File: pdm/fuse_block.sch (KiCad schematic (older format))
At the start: 14 parts, among them Q12 2N7002E, Q13 2N7002E, Q14 2N7002E, U5 BTS443P

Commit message: general changes
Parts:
- added TP6, TP7, TP8: TestPoint, TestPoint:TestPoint_THTPad_1.0x1.0mm_Drill0.5mm, symbol Connector:TestPoint
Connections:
- net Vout: now also TP7.1
- net activate: now also TP6.1
- net sense: now also TP8.1
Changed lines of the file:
@@
 $Descr A4 11693 8268
 encoding utf-8
-Sheet 6 6
+Sheet 3 6
 Title "PDM Board"
 Date "2021-01-14"
@@
 Connection ~ 7950 3600
 Wire Wire Line
-	7950 3600 9050 3600
+	7950 3600 8700 3600
 Text HLabel 9050 3600 2    50   Output ~ 0
 Vout
@@
 Connection ~ 7600 2450
 Wire Wire Line
-	7600 2450 9050 2450
-Wire Wire Line
-	3000 3700 4550 3700
+	3000 3700 3450 3700
 Wire Wire Line
 	7950 4900 8450 4900
@@
 Wire Wire Line
 	8850 3900 8850 4300
+$Comp
+L Connector:TestPoint TP7
+U 1 1 60F5EFD6
+P 8700 3300
+AR Path="/5F94FFF3/60F5EFD6" Ref="TP7"  Part="1"
+AR Path="/5F955F6E/60F5EFD6" Ref="TP4"  Part="1"
+AR Path="/5F955EE4/60F5EFD6" Ref="TP10"  Part="1"
+AR Path="/60D2AFFB/60F5EFD6" Ref="TP13"  Part="1"
+F 0 "TP13" H 8758 3418 50  0000 L CNN
+F 1 "TestPoint" H 8758 3327 50  0000 L CNN
+F 2 "TestPoint:TestPoint_THTPad_1.0x1.0mm_Drill0.5mm" H 8900 3300 50  0001 C CNN
+F 3 "~" H 8900 3300 50  0001 C CNN
+	1    8700 3300
+	1    0    0    -1
+$EndComp
+Wire Wire Line
+	8700 3300 8700 3600
+Connection ~ 8700 3600
+Wire Wire Line
+	8700 3600 9050 3600
+Wire Wire Line
+	7600 2450 8700 2450
+$Comp
+L Connector:TestPoint TP6
+U 1 1 60F62FD8
+P 8700 2150
+AR Path="/5F94FFF3/60F62FD8" Ref="TP6"  Part="1"
+AR Path="/5F955F6E/60F62FD8" Ref="TP3"  Part="1"
+AR Path="/5F955EE4/60F62FD8" Ref="TP9"  Part="1"
+AR Path="/60D2AFFB/60F62FD8" Ref="TP12"  Part="1"
+F 0 "TP12" H 8758 2268 50  0000 L CNN
+F 1 "TestPoint" H 8758 2177 50  0000 L CNN
+F 2 "TestPoint:TestPoint_THTPad_1.0x1.0mm_Drill0.5mm" H 8900 2150 50  0001 C CNN
+F 3 "~" H 8900 2150 50  0001 C CNN
+	1    8700 2150
+	1    0    0    -1
+$EndComp
+Wire Wire Line
+	8700 2150 8700 2450
+Connection ~ 8700 2450
+Wire Wire Line
+	8700 2450 9050 2450
+$Comp
+L Connector:TestPoint TP8
+U 1 1 60F647E1
+P 3450 4000
+AR Path="/5F94FFF3/60F647E1" Ref="TP8"  Part="1"
+AR Path="/5F955F6E/60F647E1" Ref="TP5"  Part="1"
+AR Path="/5F955EE4/60F647E1" Ref="TP11"  Part="1"
+AR Path="/60D2AFFB/60F647E1" Ref="TP14"  Part="1"
+F 0 "TP14" H 3392 4026 50  0000 R CNN
+F 1 "TestPoint" H 3392 4117 50  0000 R CNN
+F 2 "TestPoint:TestPoint_THTPad_1.0x1.0mm_Drill0.5mm" H 3650 4000 50  0001 C CNN
+F 3 "~" H 3650 4000 50  0001 C CNN
+	1    3450 4000
+	-1   0    0    1
+$EndComp
+Wire Wire Line
+	3450 4000 3450 3700
+Connection ~ 3450 3700
+Wire Wire Line
+	3450 3700 4550 3700
 $EndSCHEMATC

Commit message: Initial commit
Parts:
- C13: Mouser PN 603-CC0805MKX58BB105 -> 80-C0603C160J3HACTU
- D4: Mouser PN 630-HSMR-C170-R0000 -> 710-150060AS75000
- F2: Mouser PN (none) -> 652-SF-1206F500M-2
- Q12, Q13, Q14: Mouser PN (none) -> 771-2N7002NXAKR
- R13: Mouser PN 603-AC0805FR-0710K5L -> 652-CRT0603FZ2002EST
- R19, R21, R25, R29: Mouser PN (none) -> 652-CRT0603FZ2002EST
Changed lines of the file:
@@
 F 3 "~" H 7150 2850 50  0001 C CNN
 F 4 "516-3541-1-ND" H 7150 2850 50  0001 C CNN "Digi-Key_PN"
-F 5 "630-HSMR-C170-R0000" H 7150 2850 50  0001 C CNN "Mouser PN"
+F 5 "710-150060AS75000" H 7150 2850 50  0001 C CNN "Mouser PN"
 	1    7150 2850
 	0    1    1    0
@@
 F 3 "~" H 4850 3500 50  0001 C CNN
 F 4 "RNCP0805FTD10K0CT-ND" H 4850 3500 50  0001 C CNN "Digi-Key_PN"
-F 5 "603-AC0805FR-0710K5L" H 4850 3500 50  0001 C CNN "Mouser PN"
+F 5 "652-CRT0603FZ2002EST" H 4850 3500 50  0001 C CNN "Mouser PN"
 	1    4850 3500
 	0    -1   -1   0
@@
 F 3 "~" H 4550 4050 50  0001 C CNN
 F 4 "1276-1859-2-ND" H 4550 4050 50  0001 C CNN "Digi-Key_PN"
-F 5 "603-CC0805MKX58BB105" H 4550 4050 50  0001 C CNN "Mouser PN"
+F 5 "80-C0603C160J3HACTU" H 4550 4050 50  0001 C CNN "Mouser PN"
 	1    4550 4050
 	1    0    0    -1
@@
 F 3 "~" H 6650 3600 50  0001 C CNN
 F 4 "486-1688-2-ND" H 6650 3600 50  0001 C CNN "Digi-Key_PN"
+F 5 "652-SF-1206F500M-2" H 6650 3600 50  0001 C CNN "Mouser PN"
 	1    6650 3600
 	0    1    1    0
@@
 F 3 "~" H 8450 5200 50  0001 C CNN
 F 4 "RNCP0805FTD10K0CT-ND" H 8450 5200 50  0001 C CNN "Digi-Key_PN"
+F 5 "652-CRT0603FZ2002EST" H 8450 5200 50  0001 C CNN "Mouser PN"
 	1    8450 5200
 	1    0    0    -1
@@
 F 3 "~" H 3450 2600 50  0001 C CNN
 F 4 "RNCP0805FTD10K0CT-ND" H 3450 2600 50  0001 C CNN "Digi-Key_PN"
+F 5 "652-CRT0603FZ2002EST" H 3450 2600 50  0001 C CNN "Mouser PN"
 	1    3450 2600
 	1    0    0    -1
@@
 F 3 "~" H 7600 2750 50  0001 C CNN
 F 4 "RNCP0805FTD10K0CT-ND" H 7600 2750 50  0001 C CNN "Digi-Key_PN"
+F 5 "652-CRT0603FZ2002EST" H 7600 2750 50  0001 C CNN "Mouser PN"
 	1    7600 2750
 	1    0    0    -1
@@
 F 3 "~" H 8850 4450 50  0001 C CNN
 F 4 "RNCP0805FTD10K0CT-ND" H 8850 4450 50  0001 C CNN "Digi-Key_PN"
+F 5 "652-CRT0603FZ2002EST" H 8850 4450 50  0001 C CNN "Mouser PN"
 	1    8850 4450
 	1    0    0    -1
@@
 F 3 "http://www.diodes.com/assets/Datasheets/ds30376.pdf" H 8750 4900 50  0001 L CNN
 F 4 "2N7002E-FDICT-ND" H 8750 4900 50  0001 C CNN "Digi-Key_PN"
+F 5 "771-2N7002NXAKR" H 8750 4900 50  0001 C CNN "Mouser PN"
 	1    8750 4900
 	1    0    0    -1
@@
 F 3 "http://www.diodes.com/assets/Datasheets/ds30376.pdf" H 7250 2450 50  0001 L CNN
 F 4 "2N7002E-FDICT-ND" H 7250 2450 50  0001 C CNN "Digi-Key_PN"
+F 5 "771-2N7002NXAKR" H 7250 2450 50  0001 C CNN "Mouser PN"
 	1    7250 2450
 	-1   0    0    1
@@
 F 3 "http://www.diodes.com/assets/Datasheets/ds30376.pdf" H 3900 3400 50  0001 L CNN
 F 4 "2N7002E-FDICT-ND" H 3900 3400 50  0001 C CNN "Digi-Key_PN"
+F 5 "771-2N7002NXAKR" H 3900 3400 50  0001 C CNN "Mouser PN"
 	1    3900 3400
 	0    1    1    0

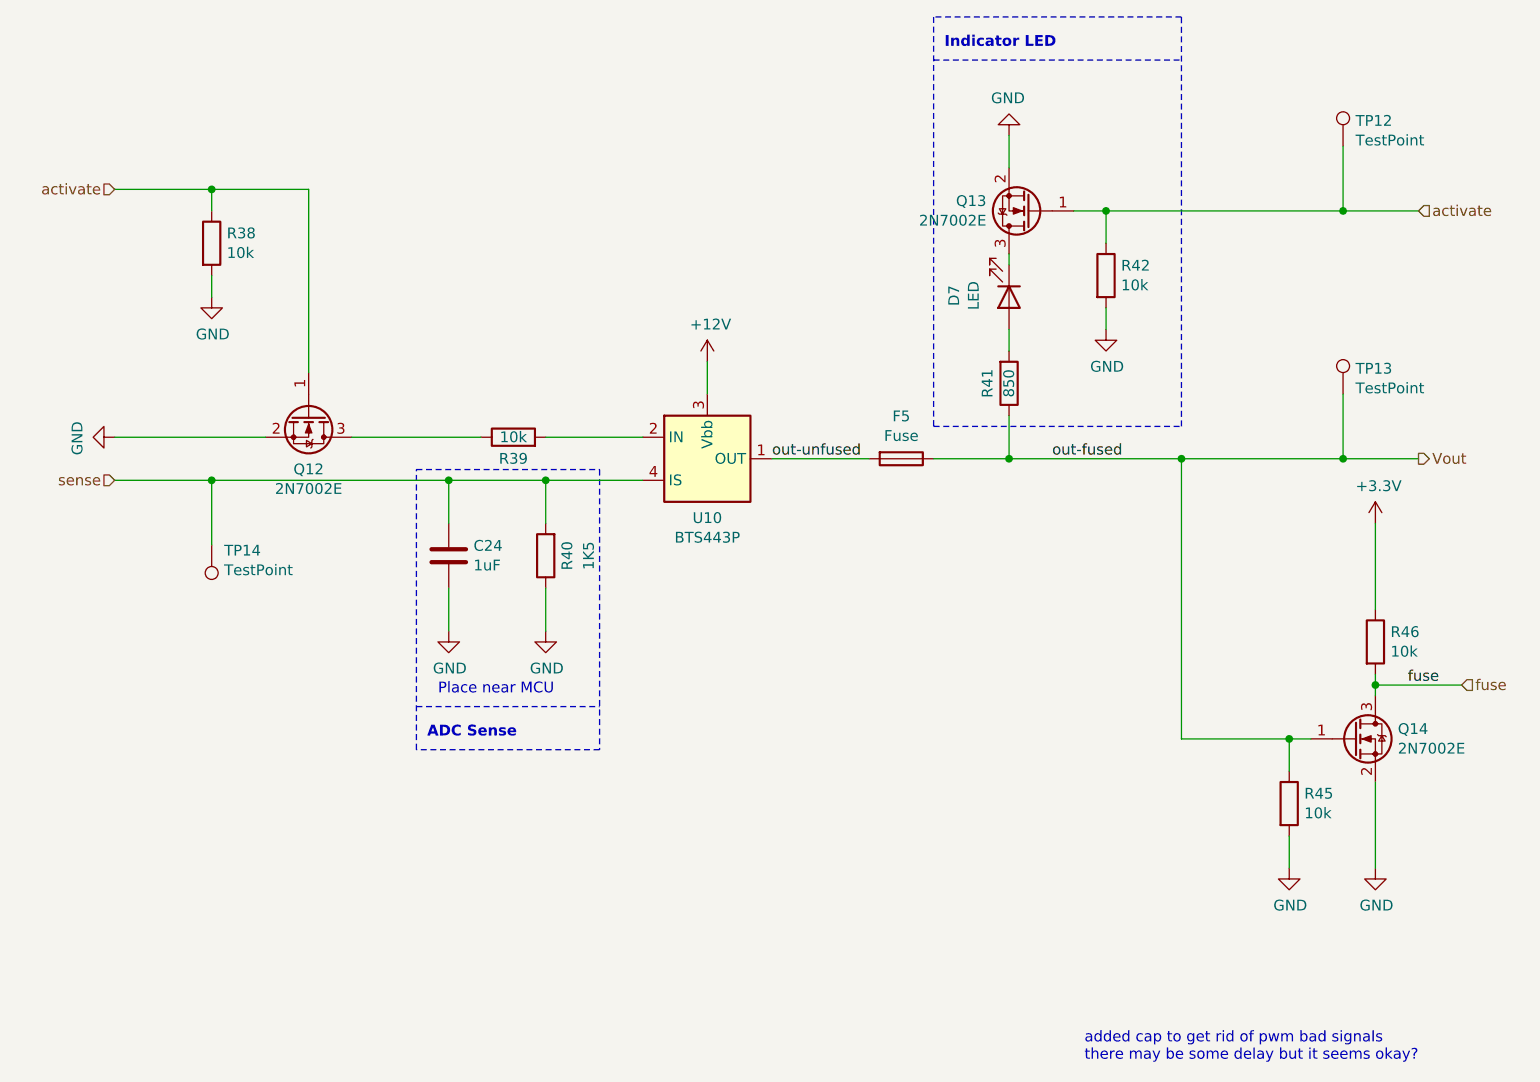
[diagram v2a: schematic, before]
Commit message: changed parts layout
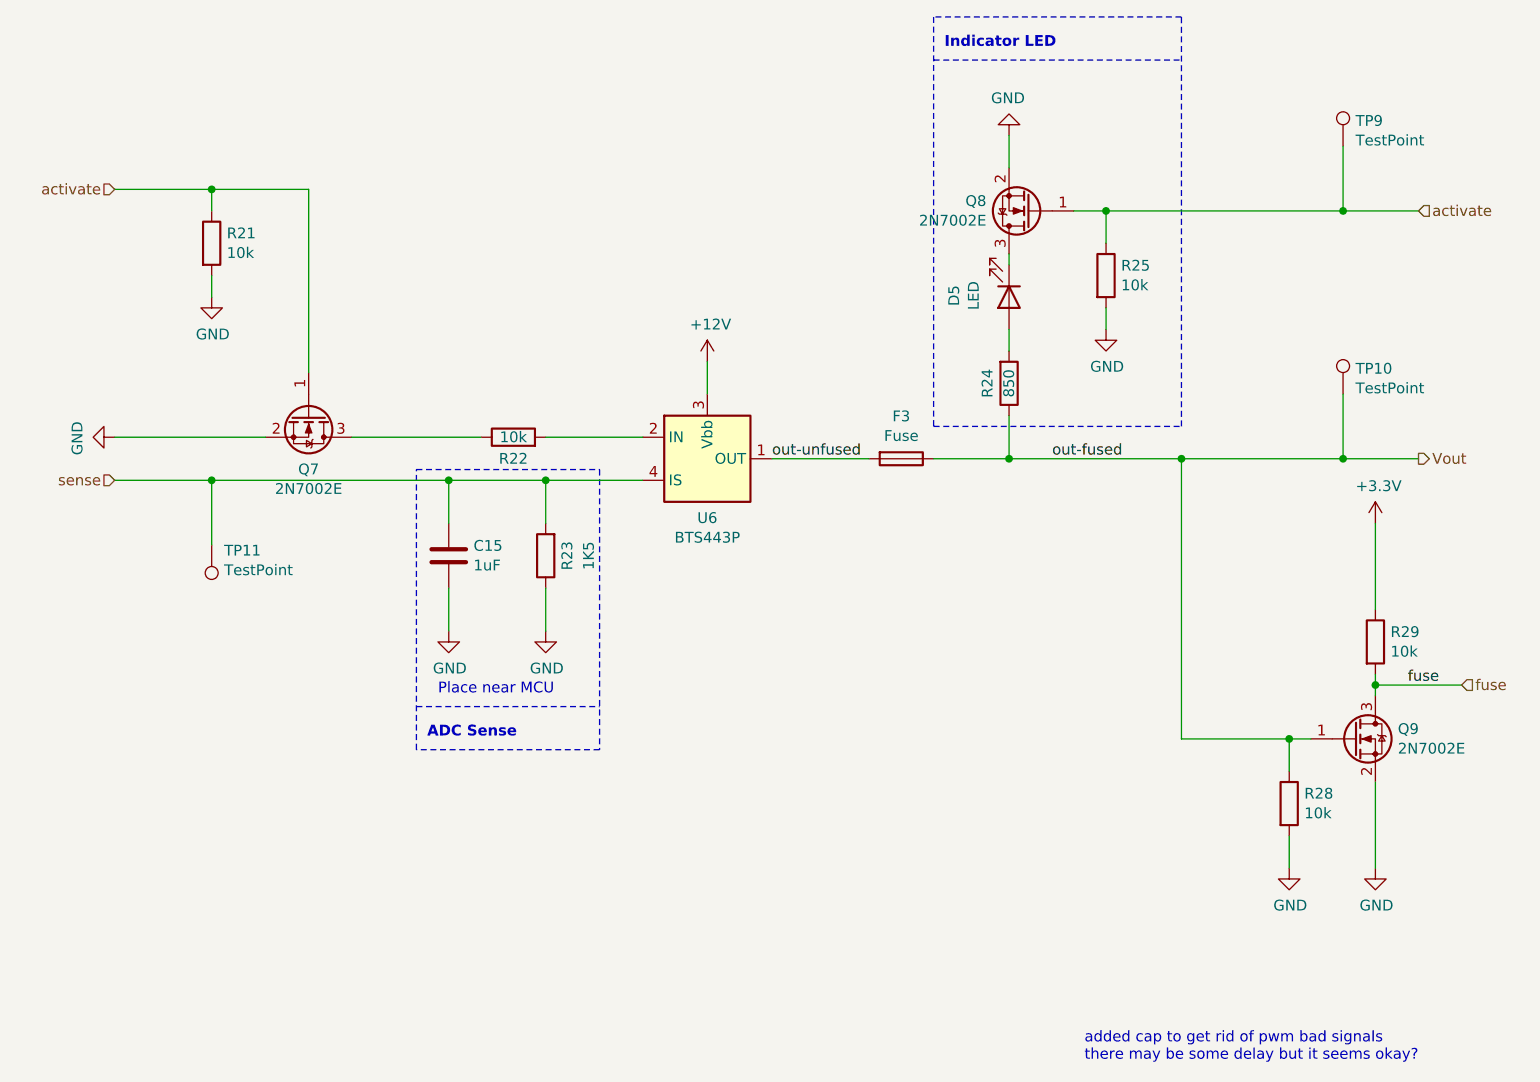
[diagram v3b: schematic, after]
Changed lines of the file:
@@
 $Descr A4 11693 8268
 encoding utf-8
-Sheet 3 6
+Sheet 4 6
 Title "PDM Board"
 Date "2021-01-14"
@@
 AR Path="/5F9560D2/5F986EB2" Ref="R?"  Part="1"
 AR Path="/60D2AFFB/5F986EB2" Ref="R41"  Part="1"
-F 0 "R41" V 7050 3250 50  0000 C CNN
+F 0 "R24" V 7050 3250 50  0000 C CNN
 F 1 "850" V 7150 3250 50  0000 C CNN
 F 2 "Resistor_SMD:R_0603_1608Metric" V 7080 3250 50  0001 C CNN
@@
 AR Path="/5F955EE4/5F98650F" Ref="D5"  Part="1"
 AR Path="/60D2AFFB/5F98650F" Ref="D7"  Part="1"
-F 0 "D7" H 7143 2595 50  0000 C CNN
+F 0 "D5" H 7143 2595 50  0000 C CNN
 F 1 "LED" H 7143 2686 50  0000 C CNN
 F 2 "LED_SMD:LED_0603_1608Metric" H 7150 2850 50  0001 C CNN
@@
 AR Path="/5F9560D2/60187A80" Ref="R?"  Part="1"
 AR Path="/60D2AFFB/60187A80" Ref="R39"  Part="1"
-F 0 "R39" V 4750 3500 50  0000 C CNN
+F 0 "R22" V 4750 3500 50  0000 C CNN
 F 1 "10k" V 4850 3500 50  0000 C CNN
 F 2 "Resistor_SMD:R_0603_1608Metric" V 4780 3500 50  0001 C CNN
@@
 AR Path="/5F955EE4/6007317B" Ref="C15"  Part="1"
 AR Path="/60D2AFFB/6007317B" Ref="C24"  Part="1"
-F 0 "C24" H 4665 4096 50  0000 L CNN
+F 0 "C15" H 4665 4096 50  0000 L CNN
 F 1 "1uF" H 4665 4005 50  0000 L CNN
 F 2 "Capacitor_SMD:C_0603_1608Metric" H 4588 3900 50  0001 C CNN
@@
 AR Path="/5F9560D2/5F95466C" Ref="F?"  Part="1"
 AR Path="/60D2AFFB/5F95466C" Ref="F5"  Part="1"
-F 0 "F5" V 6453 3600 50  0000 C CNN
+F 0 "F3" V 6453 3600 50  0000 C CNN
 F 1 "Fuse" V 6544 3600 50  0000 C CNN
 F 2 "Fuse:Fuse_1206_3216Metric" V 6580 3600 50  0001 C CNN
@@
 AR Path="/5F9560D2/5F95465A" Ref="R?"  Part="1"
 AR Path="/60D2AFFB/5F95465A" Ref="R40"  Part="1"
-F 0 "R40" V 4900 4050 50  0000 C CNN
+F 0 "R23" V 4900 4050 50  0000 C CNN
 F 1 "1K5" V 4800 4050 50  0000 C CNN
 F 2 "Resistor_SMD:R_0603_1608Metric" V 4930 4050 50  0001 C CNN
@@
 AR Path="/5F9560D2/5F95464C" Ref="U?"  Part="1"
 AR Path="/60D2AFFB/5F95464C" Ref="U10"  Part="1"
-F 0 "U10" H 5750 3325 50  0000 C CNN
+F 0 "U6" H 5750 3325 50  0000 C CNN
 F 1 "BTS443P" H 5750 3234 50  0000 C CNN
 F 2 "Package_TO_SOT_SMD:TO-252-4" H 5750 3350 50  0001 C CNN
@@
 AR Path="/5F955F6E/60F68DC5" Ref="R10"  Part="1"
 AR Path="/60D2AFFB/60F68DC5" Ref="R45"  Part="1"
-F 0 "R45" H 8520 5246 50  0000 L CNN
+F 0 "R28" H 8520 5246 50  0000 L CNN
 F 1 "10k" H 8520 5155 50  0000 L CNN
 F 2 "Resistor_SMD:R_0603_1608Metric" V 8380 5200 50  0001 C CNN
@@
 AR Path="/5F955F6E/60FAA44F" Ref="R3"  Part="1"
 AR Path="/60D2AFFB/60FAA44F" Ref="R38"  Part="1"
-F 0 "R38" H 3520 2646 50  0000 L CNN
+F 0 "R21" H 3520 2646 50  0000 L CNN
 F 1 "10k" H 3520 2555 50  0000 L CNN
 F 2 "Resistor_SMD:R_0603_1608Metric" V 3380 2600 50  0001 C CNN
@@
 AR Path="/5F955F6E/60CEC8C4" Ref="R7"  Part="1"
 AR Path="/60D2AFFB/60CEC8C4" Ref="R42"  Part="1"
-F 0 "R42" H 7670 2796 50  0000 L CNN
+F 0 "R25" H 7670 2796 50  0000 L CNN
 F 1 "10k" H 7670 2705 50  0000 L CNN
 F 2 "Resistor_SMD:R_0603_1608Metric" V 7530 2750 50  0001 C CNN
@@
 AR Path="/5F955F6E/61296EA3" Ref="R11"  Part="1"
 AR Path="/60D2AFFB/61296EA3" Ref="R46"  Part="1"
-F 0 "R46" H 8920 4496 50  0000 L CNN
+F 0 "R29" H 8920 4496 50  0000 L CNN
 F 1 "10k" H 8920 4405 50  0000 L CNN
 F 2 "Resistor_SMD:R_0603_1608Metric" V 8780 4450 50  0001 C CNN
@@
 AR Path="/5F94FFF3/60C8041A" Ref="Q6"  Part="1"
 AR Path="/5F955EE4/60C8041A" Ref="Q9"  Part="1"
-F 0 "Q14" H 8954 4946 50  0000 L CNN
+F 0 "Q9" H 8954 4946 50  0000 L CNN
 F 1 "2N7002E" H 8954 4855 50  0000 L CNN
 F 2 "Package_TO_SOT_SMD:SOT-23" H 8950 4825 50  0001 L CIN
@@
 AR Path="/5F94FFF3/60C84FB3" Ref="Q5"  Part="1"
 AR Path="/5F955EE4/60C84FB3" Ref="Q8"  Part="1"
-F 0 "Q13" H 7455 2404 50  0000 L CNN
+F 0 "Q8" H 7455 2404 50  0000 L CNN
 F 1 "2N7002E" H 7455 2495 50  0000 L CNN
 F 2 "Package_TO_SOT_SMD:SOT-23" H 7450 2375 50  0001 L CIN
@@
 AR Path="/5F94FFF3/60C8A76A" Ref="Q4"  Part="1"
 AR Path="/5F955EE4/60C8A76A" Ref="Q7"  Part="1"
-F 0 "Q12" V 4149 3400 50  0000 C CNN
+F 0 "Q7" V 4149 3400 50  0000 C CNN
 F 1 "2N7002E" V 4240 3400 50  0000 C CNN
 F 2 "Package_TO_SOT_SMD:SOT-23" H 4100 3325 50  0001 L CIN
@@
 AR Path="/5F955EE4/60F5EFD6" Ref="TP10"  Part="1"
 AR Path="/60D2AFFB/60F5EFD6" Ref="TP13"  Part="1"
-F 0 "TP13" H 8758 3418 50  0000 L CNN
+F 0 "TP10" H 8758 3418 50  0000 L CNN
 F 1 "TestPoint" H 8758 3327 50  0000 L CNN
 F 2 "TestPoint:TestPoint_THTPad_1.0x1.0mm_Drill0.5mm" H 8900 3300 50  0001 C CNN
@@
 AR Path="/5F955EE4/60F62FD8" Ref="TP9"  Part="1"
 AR Path="/60D2AFFB/60F62FD8" Ref="TP12"  Part="1"
-F 0 "TP12" H 8758 2268 50  0000 L CNN
+F 0 "TP9" H 8758 2268 50  0000 L CNN
 F 1 "TestPoint" H 8758 2177 50  0000 L CNN
 F 2 "TestPoint:TestPoint_THTPad_1.0x1.0mm_Drill0.5mm" H 8900 2150 50  0001 C CNN
@@
 AR Path="/5F955EE4/60F647E1" Ref="TP11"  Part="1"
 AR Path="/60D2AFFB/60F647E1" Ref="TP14"  Part="1"
-F 0 "TP14" H 3392 4026 50  0000 R CNN
+F 0 "TP11" H 3392 4026 50  0000 R CNN
 F 1 "TestPoint" H 3392 4117 50  0000 R CNN
 F 2 "TestPoint:TestPoint_THTPad_1.0x1.0mm_Drill0.5mm" H 3650 4000 50  0001 C CNN
